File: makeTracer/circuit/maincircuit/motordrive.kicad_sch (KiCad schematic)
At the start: 16 parts, among them J5 Motor_L, J6 Motor_R, Q1 MP4212_Q_, Q2 MP4212_Q_, U1 74HC00

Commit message: wipp
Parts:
- removed Q1, Q2: MP4212_Q_, mylibrary:MP4212_Q_WIDE, symbol SamacSys:MP4212_Q_
- added Q1, Q2: MP4212, D4jikkenLibrary:MP4212_WIDE, symbol D4jikkenLibrary:MP4212
- R5: footprint Resistor_THT:R_Axial_DIN0207_L6.3mm_D2.5mm_P10.16mm_Horizontal -> Resistor_THT:R_Axial_DIN0207_L6.3mm_D2.5mm_P5.08mm_Vertical
- R6: footprint Resistor_THT:R_Axial_DIN0207_L6.3mm_D2.5mm_P10.16mm_Horizontal -> Resistor_THT:R_Axial_DIN0207_L6.3mm_D2.5mm_P7.62mm_Horizontal
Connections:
- net GND: now also Q1.1 (S_1), Q2.1 (S_1)
- net L_SEL1: now also Q1.4 (G_2)
- net L_SEL2: now also Q1.2 (G_1)
- net R_SEL1: now also Q2.4 (G_2)
- net R_SEL2: now also Q2.2 (G_1)
- net at U1.3: now also Q1.6 (G_3)
- net at C5.1, R4.2: now also Q2.10 (S_3)
- net at C4.1, R3.2: now also Q1.10 (S_3)
- net at J6.2 (Pin_2): now also Q2.3 (D_1), Q2.7 (D_2)
- net at J6.1 (Pin_1): now also Q2.5 (S_2), Q2.9 (D_3)
- net at U1.8: now also Q2.6 (G_3)
- net at U1.11: now also Q2.8 (G_4)
- net at U1.6: now also Q1.8 (G_4)
- net at J5.1 (Pin_1): now also Q1.5 (S_2), Q1.9 (D_3)
- net at J5.2 (Pin_2): now also Q1.3 (D_1), Q1.7 (D_2)
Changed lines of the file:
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@@
       (effects (font (size 1.27 1.27)) (justify left))
     )
-    (property "Footprint" "Resistor_THT:R_Axial_DIN0207_L6.3mm_D2.5mm_P10.16mm_Horizontal" (at 29.972 92.075 90)
+    (property "Footprint" "Resistor_THT:R_Axial_DIN0207_L6.3mm_D2.5mm_P5.08mm_Vertical" (at 29.972 92.075 90)
       (effects (font (size 1.27 1.27)) hide)
     )
@@
       (effects (font (size 1.27 1.27)) (justify left))
     )
-    (property "Footprint" "Resistor_THT:R_Axial_DIN0207_L6.3mm_D2.5mm_P10.16mm_Horizontal" (at 36.322 92.075 90)
+    (property "Footprint" "Resistor_THT:R_Axial_DIN0207_L6.3mm_D2.5mm_P7.62mm_Horizontal" (at 36.322 92.075 90)
       (effects (font (size 1.27 1.27)) hide)
     )
@@
         (path "/a588b4f4-c52b-4b14-933c-cea644bb9512/c849bbbd-6991-4135-9c62-ffd8842098ea"
           (reference "R4") (unit 1)
-        )
-      )
-    )
-  )
-  (symbol (lib_id "SamacSys:MP4212_Q_") (at 209.55 44.45 90) (unit 1)
-    (in_bom yes) (on_board yes) (dnp no) (fields_autoplaced)
-    (property "Reference" "Q2" (at 236.22 31.75 90)
-      (effects (font (size 1.27 1.27)) (justify right))
-    )
-    (property "Value" "MP4212_Q_" (at 236.22 34.29 90)
-      (effects (font (size 1.27 1.27)) (justify right))
-    )
-    (property "Footprint" "mylibrary:MP4212_Q_WIDE" (at 207.01 25.4 0)
-      (effects (font (size 1.27 1.27)) (justify left) hide)
-    )
-    (property "Datasheet" "https://toshiba-semicon-storage.com/info/docget.jsp?did=15989&prodName=MP4212" (at 209.55 25.4 0)
-      (effects (font (size 1.27 1.27)) (justify left) hide)
-    )
-    (property "Description" "Quad N/P-Channel MOSFET Module, 5 A, 60 V, 10-Pin SIP" (at 212.09 25.4 0)
-      (effects (font (size 1.27 1.27)) (justify left) hide)
-    )
-    (property "Height" "9.2" (at 214.63 25.4 0)
-      (effects (font (size 1.27 1.27)) (justify left) hide)
-    )
-    (property "RS Part Number" "6012958" (at 217.17 25.4 0)
-      (effects (font (size 1.27 1.27)) (justify left) hide)
-    )
-    (property "RS Price/Stock" "https://uk.rs-online.com/web/p/products/6012958" (at 219.71 25.4 0)
-      (effects (font (size 1.27 1.27)) (justify left) hide)
-    )
-    (property "Manufacturer_Name" "Toshiba" (at 222.25 25.4 0)
-      (effects (font (size 1.27 1.27)) (justify left) hide)
-    )
-    (property "Manufacturer_Part_Number" "MP4212(Q)" (at 224.79 25.4 0)
-      (effects (font (size 1.27 1.27)) (justify left) hide)
-    )
-    (pin "1")
-    (pin "10")
-    (pin "2")
-    (pin "3")
-    (pin "4")
-    (pin "5")
-    (pin "6")
-    (pin "7")
-    (pin "8")
-    (pin "9")
-    (instances
-      (project "maincircuit"
-        (path "/a588b4f4-c52b-4b14-933c-cea644bb9512/c849bbbd-6991-4135-9c62-ffd8842098ea"
-          (reference "Q2") (unit 1)
         )
       )
@@
     )
   )
-  (symbol (lib_id "power:GND") (at 44.45 101.6 0) (unit 1)
-    (in_bom yes) (on_board yes) (dnp no) (fields_autoplaced)
-    (property "Reference" "#PWR027" (at 44.45 107.95 0)
-      (effects (font (size 1.27 1.27)) hide)
-    )
-    (property "Value" "GND" (at 44.45 106.68 0)
-      (effects (font (size 1.27 1.27)))
-    )
-    (property "Footprint" "" (at 44.45 101.6 0)
-      (effects (font (size 1.27 1.27)) hide)
-    )
-    (property "Datasheet" "" (at 44.45 101.6 0)
-      (effects (font (size 1.27 1.27)) hide)
-    )
-    (pin "1")
-    (instances
-      (project "maincircuit"
-        (path "/a588b4f4-c52b-4b14-933c-cea644bb9512/c849bbbd-6991-4135-9c62-ffd8842098ea"
-          (reference "#PWR027") (unit 1)
-        )
-      )
-    )
-  )
-  (symbol (lib_id "SamacSys:MP4212_Q_") (at 82.55 44.45 90) (unit 1)
+  (symbol (lib_id "D4jikkenLibrary:MP4212") (at 82.55 44.45 90) (unit 1)
     (in_bom yes) (on_board yes) (dnp no) (fields_autoplaced)
     (property "Reference" "Q1" (at 109.22 31.75 90)
       (effects (font (size 1.27 1.27)) (justify right))
     )
-    (property "Value" "MP4212_Q_" (at 109.22 34.29 90)
+    (property "Value" "MP4212" (at 109.22 34.29 90)
       (effects (font (size 1.27 1.27)) (justify right))
     )
-    (property "Footprint" "mylibrary:MP4212_Q_WIDE" (at 80.01 25.4 0)
-      (effects (font (size 1.27 1.27)) (justify left) hide)
-    )
-    (property "Datasheet" "https://toshiba-semicon-storage.com/info/docget.jsp?did=15989&prodName=MP4212" (at 82.55 25.4 0)
-      (effects (font (size 1.27 1.27)) (justify left) hide)
-    )
-    (property "Description" "Quad N/P-Channel MOSFET Module, 5 A, 60 V, 10-Pin SIP" (at 85.09 25.4 0)
-      (effects (font (size 1.27 1.27)) (justify left) hide)
-    )
-    (property "Height" "9.2" (at 87.63 25.4 0)
-      (effects (font (size 1.27 1.27)) (justify left) hide)
-    )
-    (property "RS Part Number" "6012958" (at 90.17 25.4 0)
-      (effects (font (size 1.27 1.27)) (justify left) hide)
-    )
-    (property "RS Price/Stock" "https://uk.rs-online.com/web/p/products/6012958" (at 92.71 25.4 0)
-      (effects (font (size 1.27 1.27)) (justify left) hide)
-    )
-    (property "Manufacturer_Name" "Toshiba" (at 95.25 25.4 0)
-      (effects (font (size 1.27 1.27)) (justify left) hide)
-    )
-    (property "Manufacturer_Part_Number" "MP4212(Q)" (at 97.79 25.4 0)
-      (effects (font (size 1.27 1.27)) (justify left) hide)
+    (property "Footprint" "D4jikkenLibrary:MP4212_WIDE" (at 109.22 35.56 90)
+      (effects (font (size 1.27 1.27)) (justify right) hide)
+    )
+    (property "Datasheet" "https://toshiba.semicon-storage.com/info/MP4212_datasheet_en_20061027.pdf?did=15989&prodName=MP4212" (at 82.55 44.45 0)
+      (effects (font (size 1.27 1.27)) hide)
     )
     (pin "1")
@@
         )
       )
+    )
+  )
+  (symbol (lib_id "power:GND") (at 44.45 101.6 0) (unit 1)
+    (in_bom yes) (on_board yes) (dnp no) (fields_autoplaced)
+    (property "Reference" "#PWR027" (at 44.45 107.95 0)
+      (effects (font (size 1.27 1.27)) hide)
+    )
+    (property "Value" "GND" (at 44.45 106.68 0)
+      (effects (font (size 1.27 1.27)))
+    )
+    (property "Footprint" "" (at 44.45 101.6 0)
+      (effects (font (size 1.27 1.27)) hide)
+    )
+    (property "Datasheet" "" (at 44.45 101.6 0)
+      (effects (font (size 1.27 1.27)) hide)
+    )
+    (pin "1")
+    (instances
+      (project "maincircuit"
+        (path "/a588b4f4-c52b-4b14-933c-cea644bb9512/c849bbbd-6991-4135-9c62-ffd8842098ea"
+          (reference "#PWR027") (unit 1)
+        )
+      )
+    )
+  )
+  (symbol (lib_id "D4jikkenLibrary:MP4212") (at 209.55 44.45 90) (unit 1)
+    (in_bom yes) (on_board yes) (dnp no) (fields_autoplaced)
+    (property "Reference" "Q2" (at 236.22 31.75 90)
+      (effects (font (size 1.27 1.27)) (justify right))
+    )
+    (property "Value" "MP4212" (at 236.22 34.29 90)
+      (effects (font (size 1.27 1.27)) (justify right))
+    )
+    (property "Footprint" "D4jikkenLibrary:MP4212_WIDE" (at 209.55 44.45 0)
+      (effects (font (size 1.27 1.27)) hide)
+    )
+    (property "Datasheet" "https://toshiba.semicon-storage.com/info/MP4212_datasheet_en_20061027.pdf?did=15989&prodName=MP4212" (at 209.55 44.45 0)
+      (effects (font (size 1.27 1.27)) hide)
+    )
+    (pin "1")
+    (pin "10")
+    (pin "2")
+    (pin "3")
+    (pin "4")
+    (pin "5")
+    (pin "6")
+    (pin "7")
+    (pin "8")
+    (pin "9")
+    (instances
+      (project "maincircuit"
+        (path "/a588b4f4-c52b-4b14-933c-cea644bb9512/c849bbbd-6991-4135-9c62-ffd8842098ea"
+          (reference "Q2") (unit 1)
+        )
+      )

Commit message: done: maincircuit
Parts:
- R10, R8: footprint Resistor_THT:R_Axial_DIN0207_L6.3mm_D2.5mm_P10.16mm_Horizontal -> Resistor_THT:R_Axial_DIN0207_L6.3mm_D2.5mm_P15.24mm_Horizontal
- R6: footprint Resistor_THT:R_Axial_DIN0207_L6.3mm_D2.5mm_P7.62mm_Horizontal -> Resistor_THT:R_Axial_DIN0207_L6.3mm_D2.5mm_P10.16mm_Horizontal
- R7: footprint Resistor_THT:R_Axial_DIN0207_L6.3mm_D2.5mm_P10.16mm_Horizontal -> Resistor_THT:R_Axial_DIN0207_L6.3mm_D2.5mm_P7.62mm_Horizontal
- R9: footprint Resistor_THT:R_Axial_DIN0207_L6.3mm_D2.5mm_P10.16mm_Horizontal -> Resistor_THT:R_Axial_DIN0207_L6.3mm_D2.5mm_P5.08mm_Vertical
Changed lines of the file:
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@@
       (effects (font (size 1.27 1.27)) (justify left))
     )
-    (property "Footprint" "Resistor_THT:R_Axial_DIN0207_L6.3mm_D2.5mm_P10.16mm_Horizontal" (at 163.322 92.075 90)
+    (property "Footprint" "Resistor_THT:R_Axial_DIN0207_L6.3mm_D2.5mm_P5.08mm_Vertical" (at 163.322 92.075 90)
       (effects (font (size 1.27 1.27)) hide)
     )
@@
       (effects (font (size 1.27 1.27)) (justify left))
     )
-    (property "Footprint" "Resistor_THT:R_Axial_DIN0207_L6.3mm_D2.5mm_P10.16mm_Horizontal" (at 42.672 92.075 90)
+    (property "Footprint" "Resistor_THT:R_Axial_DIN0207_L6.3mm_D2.5mm_P7.62mm_Horizontal" (at 42.672 92.075 90)
       (effects (font (size 1.27 1.27)) hide)
     )
@@
       (effects (font (size 1.27 1.27)) (justify left))
     )
-    (property "Footprint" "Resistor_THT:R_Axial_DIN0207_L6.3mm_D2.5mm_P7.62mm_Horizontal" (at 36.322 92.075 90)
+    (property "Footprint" "Resistor_THT:R_Axial_DIN0207_L6.3mm_D2.5mm_P10.16mm_Horizontal" (at 36.322 92.075 90)
       (effects (font (size 1.27 1.27)) hide)
     )
@@
       (effects (font (size 1.27 1.27)) (justify left))
     )
-    (property "Footprint" "Resistor_THT:R_Axial_DIN0207_L6.3mm_D2.5mm_P10.16mm_Horizontal" (at 169.672 92.075 90)
+    (property "Footprint" "Resistor_THT:R_Axial_DIN0207_L6.3mm_D2.5mm_P15.24mm_Horizontal" (at 169.672 92.075 90)
       (effects (font (size 1.27 1.27)) hide)
     )
@@
       (effects (font (size 1.27 1.27)) (justify left))
     )
-    (property "Footprint" "Resistor_THT:R_Axial_DIN0207_L6.3mm_D2.5mm_P10.16mm_Horizontal" (at 156.972 92.075 90)
-      (effects (font (size 1.27 1.27)) hide)
-    )
+    (property "Footprint" "Resistor_THT:R_Axial_DIN0207_L6.3mm_D2.5mm_P15.24mm_Horizontal" (at 156.972 92.075 90)
+      (effects (font (size 1.27 1.27)) hide)
+    )

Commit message: fix: yabai jumper
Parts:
- R10, R8: footprint Resistor_THT:R_Axial_DIN0207_L6.3mm_D2.5mm_P15.24mm_Horizontal -> Resistor_THT:R_Axial_DIN0207_L6.3mm_D2.5mm_P7.62mm_Horizontal
- R3: footprint Resistor_THT:R_Axial_DIN0309_L9.0mm_D3.2mm_P12.70mm_Horizontal -> Resistor_THT:R_Axial_DIN0309_L9.0mm_D3.2mm_P20.32mm_Horizontal
- R5: footprint Resistor_THT:R_Axial_DIN0207_L6.3mm_D2.5mm_P5.08mm_Vertical -> Resistor_THT:R_Axial_DIN0207_L6.3mm_D2.5mm_P7.62mm_Horizontal
- R7: footprint Resistor_THT:R_Axial_DIN0207_L6.3mm_D2.5mm_P7.62mm_Horizontal -> Resistor_THT:R_Axial_DIN0207_L6.3mm_D2.5mm_P10.16mm_Horizontal
- R9: footprint Resistor_THT:R_Axial_DIN0207_L6.3mm_D2.5mm_P5.08mm_Vertical -> Resistor_THT:R_Axial_DIN0207_L6.3mm_D2.5mm_P2.54mm_Vertical
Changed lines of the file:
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@@
       (effects (font (size 1.27 1.27)) (justify left))
     )
-    (property "Footprint" "Resistor_THT:R_Axial_DIN0207_L6.3mm_D2.5mm_P5.08mm_Vertical" (at 163.322 92.075 90)
+    (property "Footprint" "Resistor_THT:R_Axial_DIN0207_L6.3mm_D2.5mm_P2.54mm_Vertical" (at 163.322 92.075 90)
       (effects (font (size 1.27 1.27)) hide)
     )
@@
       (effects (font (size 1.27 1.27)) (justify left))
     )
-    (property "Footprint" "Resistor_THT:R_Axial_DIN0207_L6.3mm_D2.5mm_P7.62mm_Horizontal" (at 42.672 92.075 90)
+    (property "Footprint" "Resistor_THT:R_Axial_DIN0207_L6.3mm_D2.5mm_P10.16mm_Horizontal" (at 42.672 92.075 90)
       (effects (font (size 1.27 1.27)) hide)
     )
@@
       (effects (font (size 1.27 1.27)) (justify left))
     )
-    (property "Footprint" "Resistor_THT:R_Axial_DIN0207_L6.3mm_D2.5mm_P5.08mm_Vertical" (at 29.972 92.075 90)
+    (property "Footprint" "Resistor_THT:R_Axial_DIN0207_L6.3mm_D2.5mm_P7.62mm_Horizontal" (at 29.972 92.075 90)
       (effects (font (size 1.27 1.27)) hide)
     )
@@
       (effects (font (size 1.27 1.27)) (justify left))
     )
-    (property "Footprint" "Resistor_THT:R_Axial_DIN0207_L6.3mm_D2.5mm_P15.24mm_Horizontal" (at 169.672 92.075 90)
+    (property "Footprint" "Resistor_THT:R_Axial_DIN0207_L6.3mm_D2.5mm_P7.62mm_Horizontal" (at 169.672 92.075 90)
       (effects (font (size 1.27 1.27)) hide)
     )
@@
       (effects (font (size 1.27 1.27)) (justify left))
     )
-    (property "Footprint" "Resistor_THT:R_Axial_DIN0207_L6.3mm_D2.5mm_P15.24mm_Horizontal" (at 156.972 92.075 90)
+    (property "Footprint" "Resistor_THT:R_Axial_DIN0207_L6.3mm_D2.5mm_P7.62mm_Horizontal" (at 156.972 92.075 90)
       (effects (font (size 1.27 1.27)) hide)
     )
@@
       (effects (font (size 1.27 1.27)) (justify left))
     )
-    (property "Footprint" "Resistor_THT:R_Axial_DIN0309_L9.0mm_D3.2mm_P12.70mm_Horizontal" (at 125.222 38.1 90)
-      (effects (font (size 1.27 1.27)) hide)
-    )
+    (property "Footprint" "Resistor_THT:R_Axial_DIN0309_L9.0mm_D3.2mm_P20.32mm_Horizontal" (at 125.222 38.1 90)
+      (effects (font (size 1.27 1.27)) hide)
+    )

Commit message: complete: circuit
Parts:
- R3: footprint Resistor_THT:R_Axial_DIN0309_L9.0mm_D3.2mm_P20.32mm_Horizontal -> Resistor_THT:R_Axial_DIN0309_L9.0mm_D3.2mm_P12.70mm_Horizontal
- R4: footprint Resistor_THT:R_Axial_DIN0309_L9.0mm_D3.2mm_P12.70mm_Horizontal -> Resistor_THT:R_Axial_DIN0309_L9.0mm_D3.2mm_P25.40mm_Horizontal
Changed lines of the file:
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@@
       (effects (font (size 1.27 1.27)) (justify left))
     )
-    (property "Footprint" "Resistor_THT:R_Axial_DIN0309_L9.0mm_D3.2mm_P12.70mm_Horizontal" (at 252.222 38.1 90)
+    (property "Footprint" "Resistor_THT:R_Axial_DIN0309_L9.0mm_D3.2mm_P25.40mm_Horizontal" (at 252.222 38.1 90)
       (effects (font (size 1.27 1.27)) hide)
     )
@@
       (effects (font (size 1.27 1.27)) (justify left))
     )
-    (property "Footprint" "Resistor_THT:R_Axial_DIN0309_L9.0mm_D3.2mm_P20.32mm_Horizontal" (at 125.222 38.1 90)
-      (effects (font (size 1.27 1.27)) hide)
-    )
+    (property "Footprint" "Resistor_THT:R_Axial_DIN0309_L9.0mm_D3.2mm_P12.70mm_Horizontal" (at 125.222 38.1 90)
+      (effects (font (size 1.27 1.27)) hide)
+    )

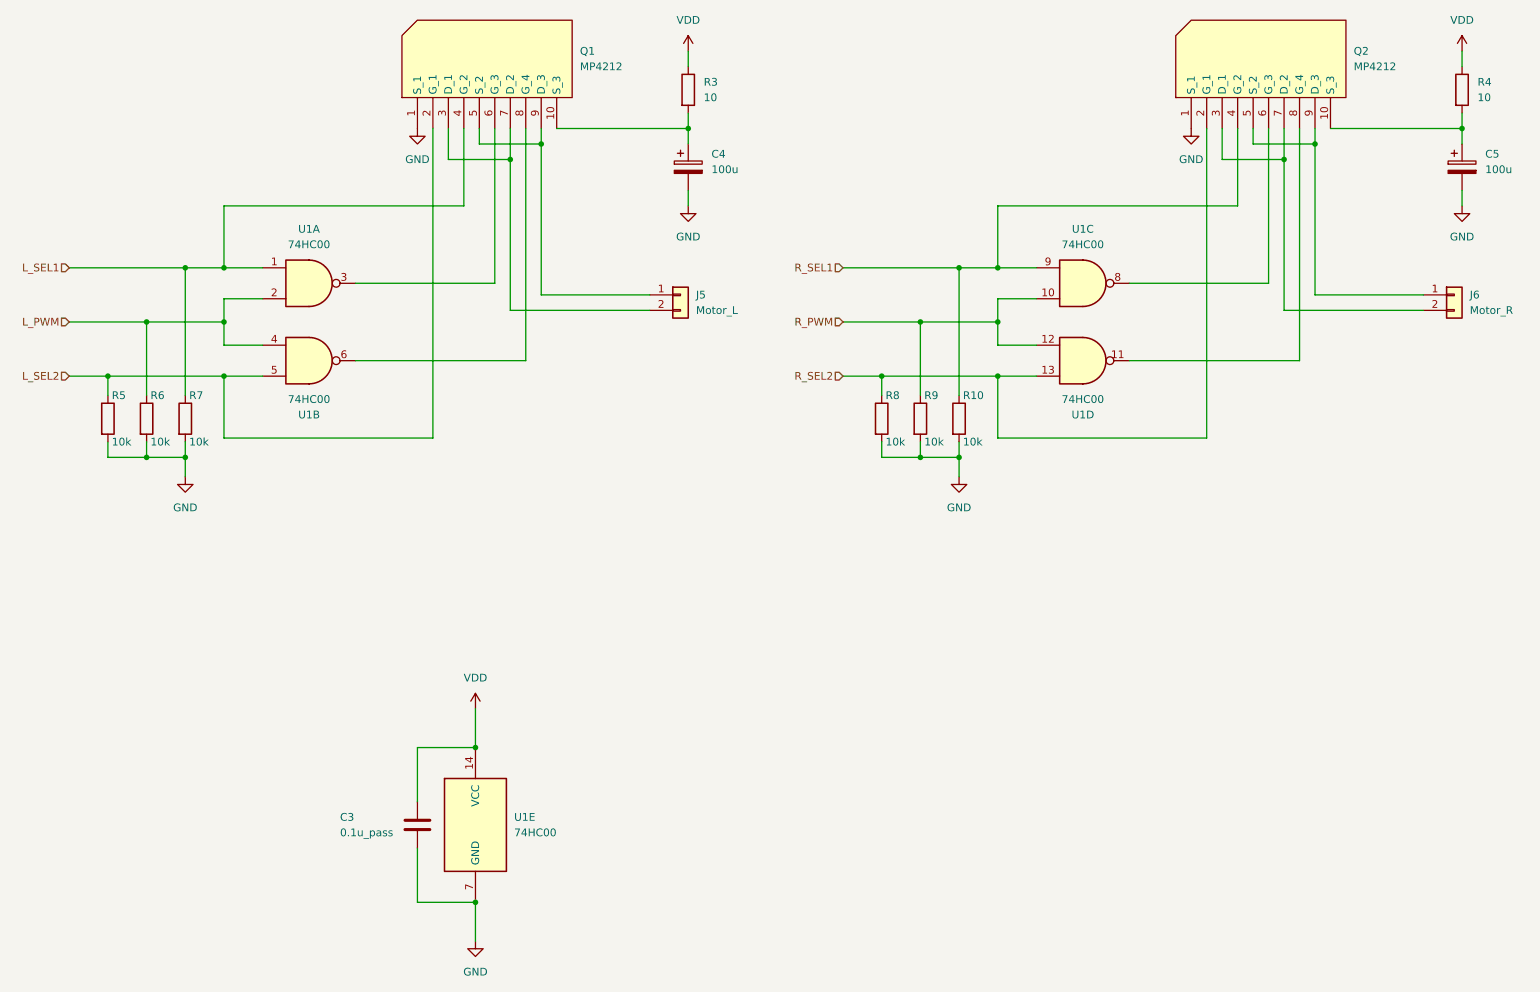
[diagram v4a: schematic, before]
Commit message: fix: .2mm to .4mm
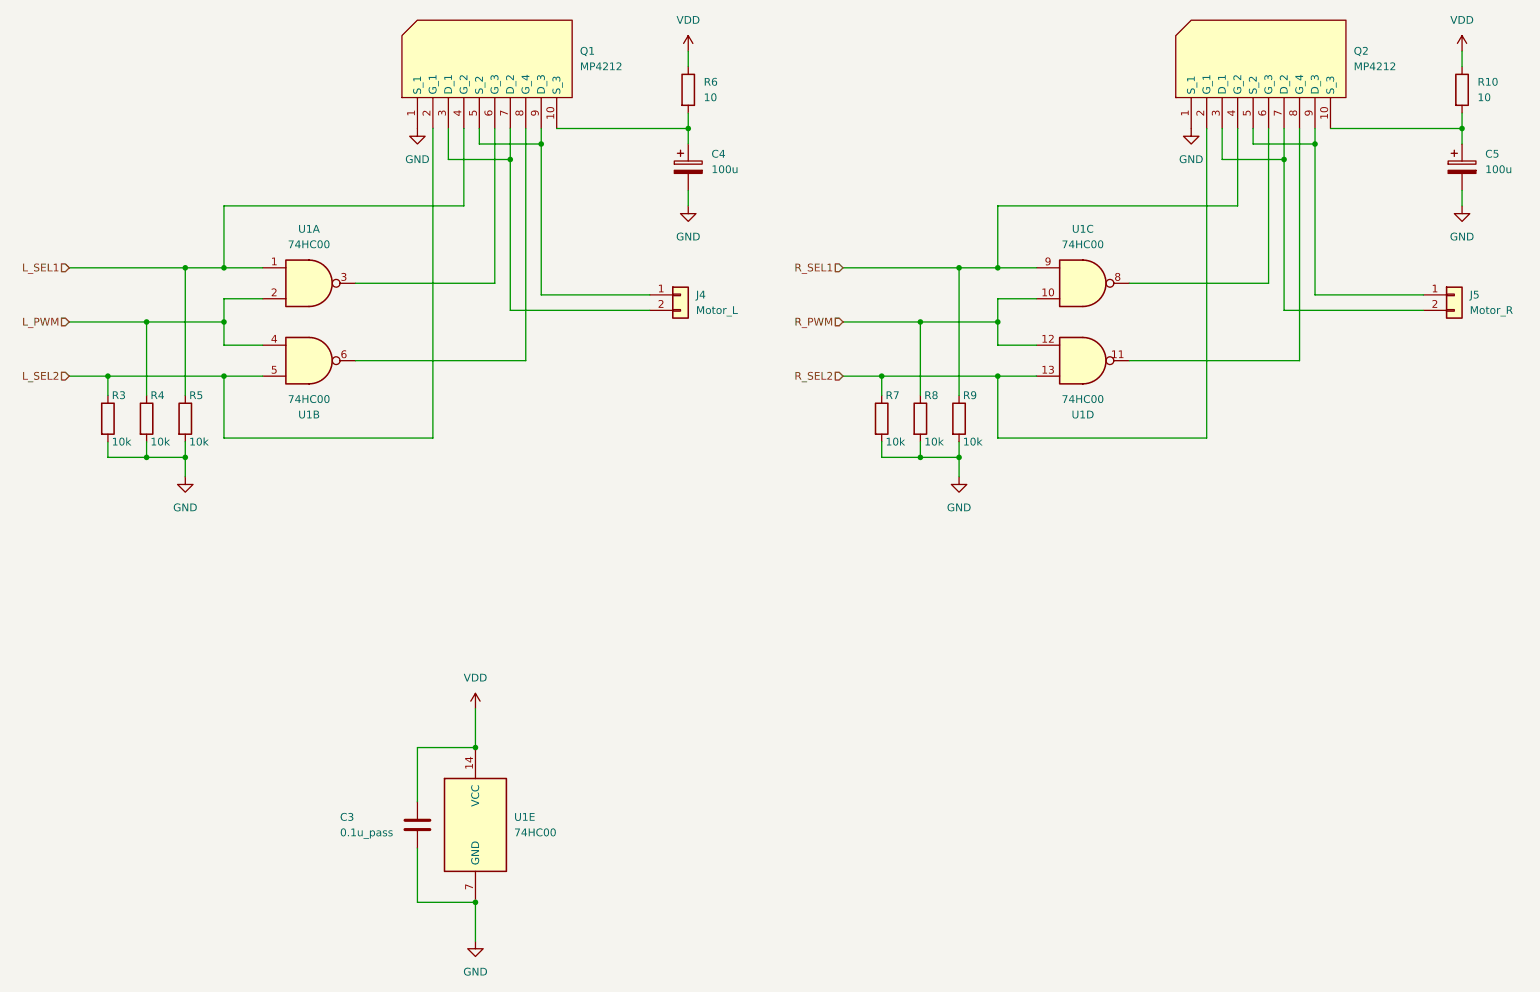
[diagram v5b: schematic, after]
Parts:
- R10: renamed from R4; footprint Resistor_THT:R_Axial_DIN0309_L9.0mm_D3.2mm_P25.40mm_Horizontal -> Resistor_THT:R_Axial_DIN0309_L9.0mm_D3.2mm_P12.70mm_Horizontal
- R4: renamed from R6; footprint Resistor_THT:R_Axial_DIN0207_L6.3mm_D2.5mm_P10.16mm_Horizontal -> Resistor_THT:R_Axial_DIN0207_L6.3mm_D2.5mm_P7.62mm_Horizontal
- R5: renamed from R7; footprint Resistor_THT:R_Axial_DIN0207_L6.3mm_D2.5mm_P10.16mm_Horizontal -> Resistor_THT:R_Axial_DIN0207_L6.3mm_D2.5mm_P5.08mm_Vertical
- R6: renamed from R3; footprint Resistor_THT:R_Axial_DIN0309_L9.0mm_D3.2mm_P12.70mm_Horizontal -> Resistor_THT:R_Axial_DIN0309_L9.0mm_D3.2mm_P20.32mm_Horizontal
- R9: renamed from R10; footprint Resistor_THT:R_Axial_DIN0207_L6.3mm_D2.5mm_P7.62mm_Horizontal -> Resistor_THT:R_Axial_DIN0207_L6.3mm_D2.5mm_P2.54mm_Vertical
- renumbered J5 to J4, J6 to J5, R5 to R3, R8 to R7, R9 to R8
